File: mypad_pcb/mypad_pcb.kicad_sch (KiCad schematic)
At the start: 25 parts, among them J1 USB_C_Receptacle_USB2.0, SW1 SW_BOOTMODE, SW2 SW_RESET, U1 FT232RL, U2 AMS1117-3.3, U3 STM32F030K6Tx, Y1 16MHz

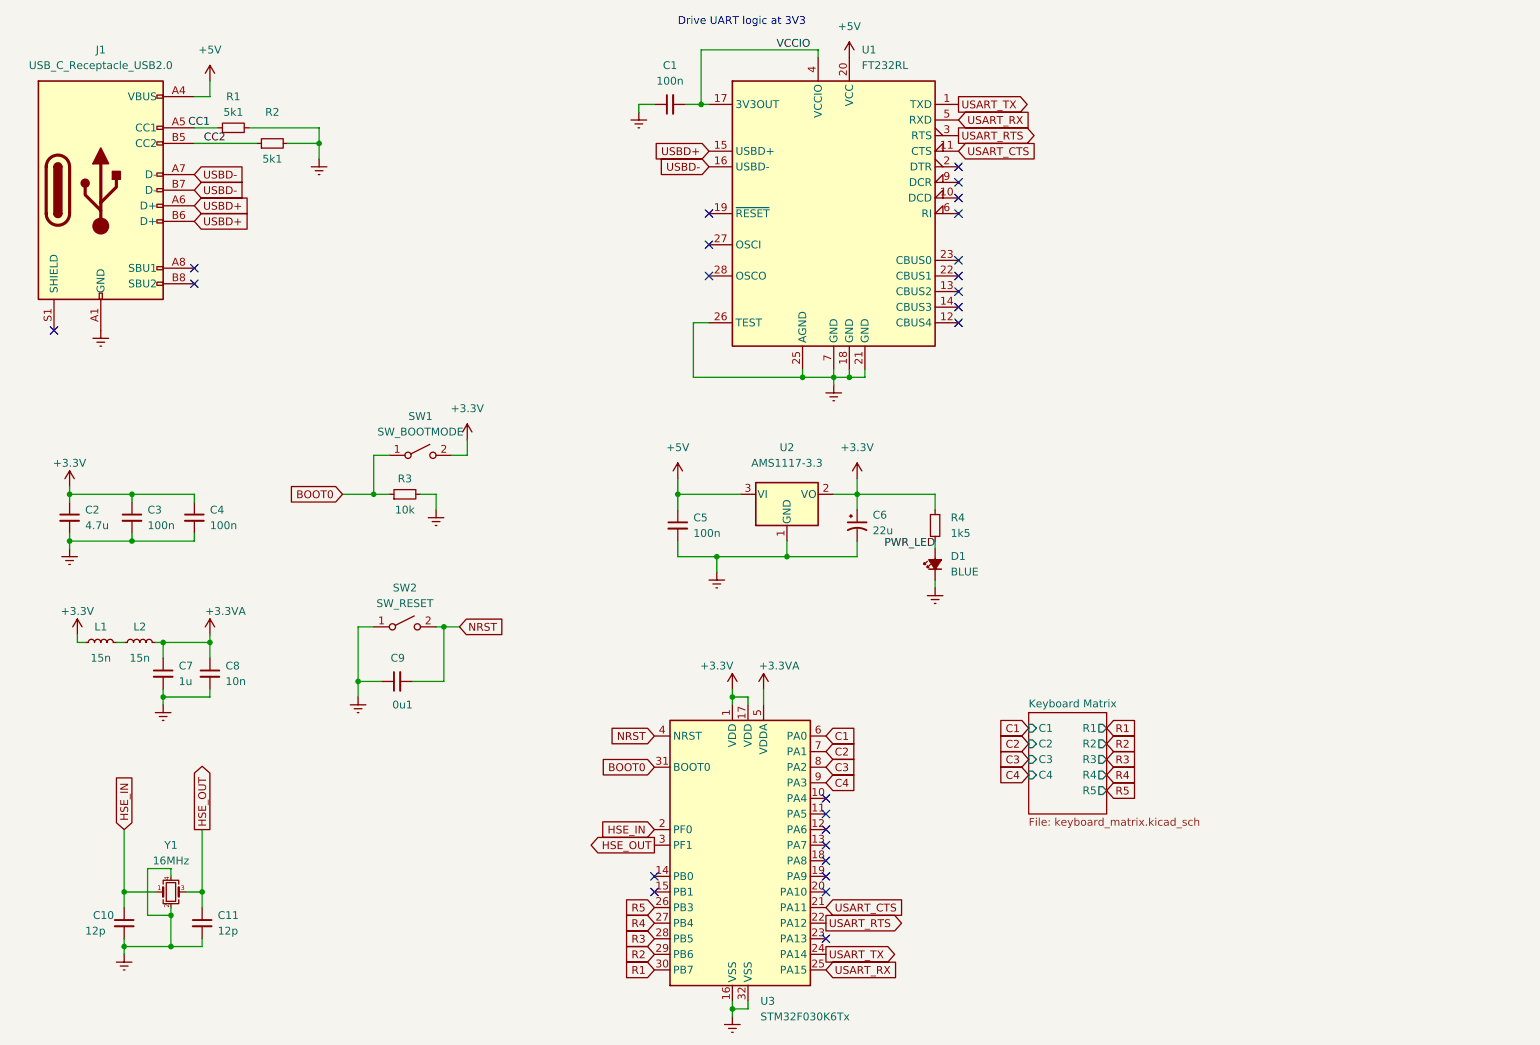
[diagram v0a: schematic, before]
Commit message: Swap components for STM32F042C6 compatible ones
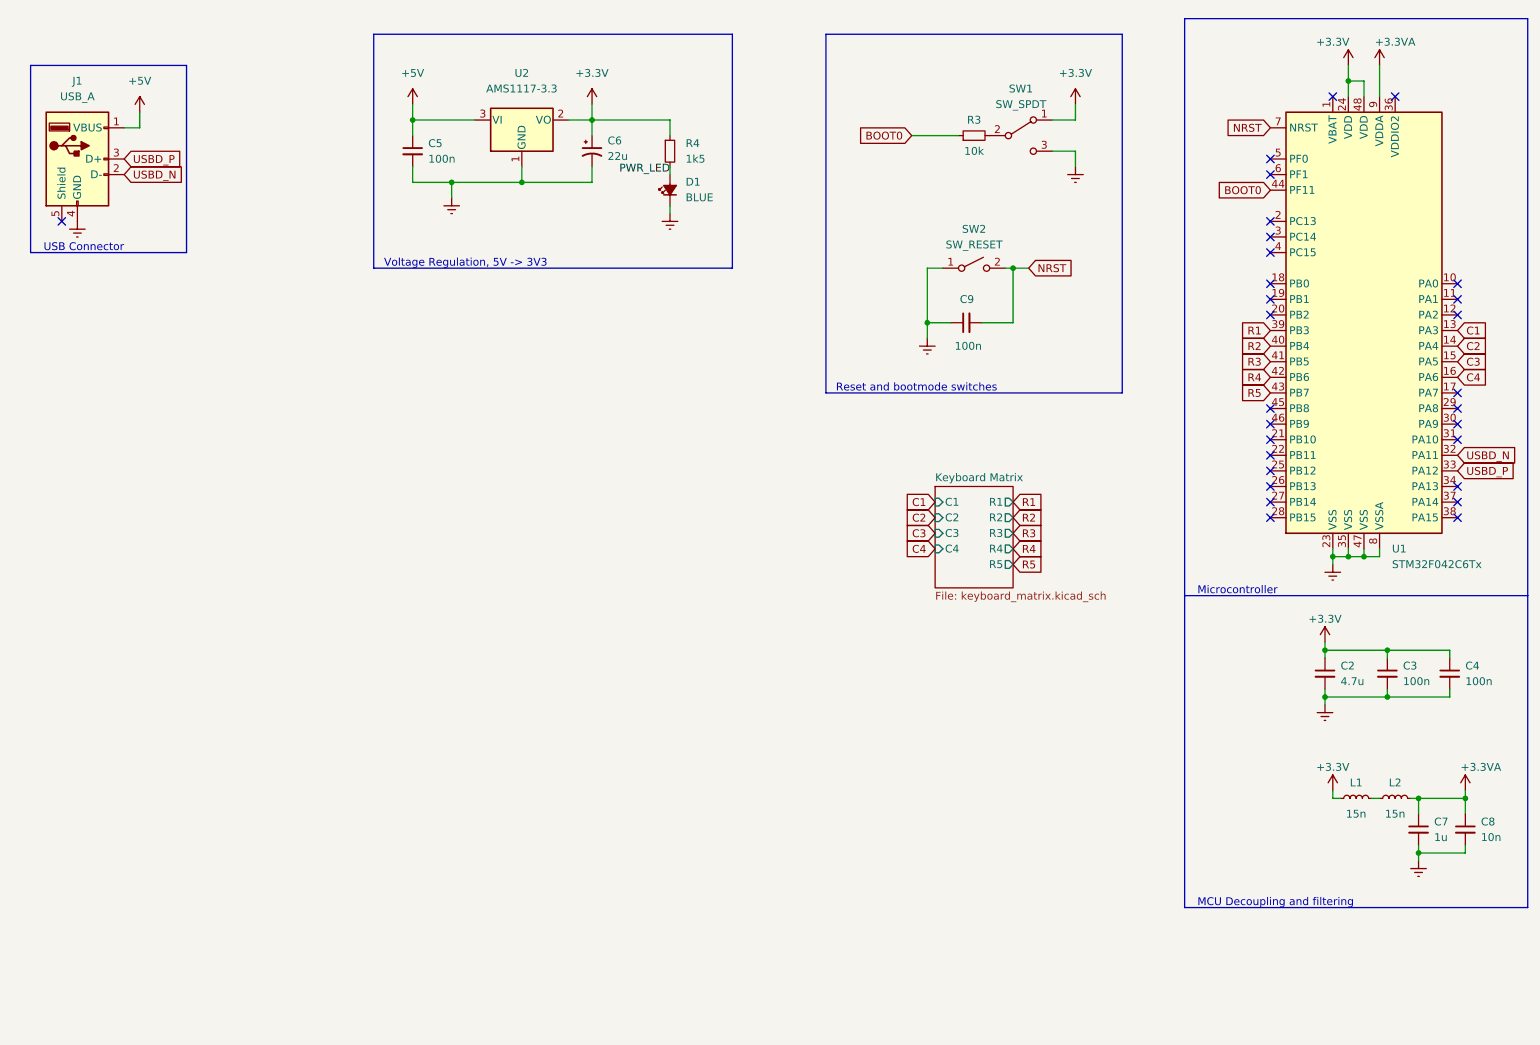
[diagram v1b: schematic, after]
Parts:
- removed C1: 100n, Capacitor_SMD:C_0603_1608Metric, symbol Device:C_Small
- removed C10, C11: 12p, Capacitor_SMD:C_0603_1608Metric, symbol Device:C_Small
- removed J1: USB_C_Receptacle_USB2.0, Connector_USB:USB_C_Receptacle_HRO_TYPE-C-31-M-12, symbol Connector:USB_C_Receptacle_USB2.0
- removed R1, R2: 5k1, Resistor_SMD:R_0603_1608Metric, symbol Device:R_Small
- removed SW1: SW_BOOTMODE, Button_Switch_THT:SW_PUSH_6mm, symbol Switch:SW_SPST
- removed U1: FT232RL, Package_SO:SSOP-28_5.3x10.2mm_P0.65mm, symbol Interface_USB:FT232RL
- removed U3: STM32F030K6Tx, Package_QFP:LQFP-32_7x7mm_P0.8mm, symbol MCU_ST_STM32F0:STM32F030K6Tx
- removed Y1: 16MHz, Crystal:Crystal_SMD_3225-4Pin_3.2x2.5mm, symbol Device:Crystal_GND24_Small
- added J1: USB_A, Connector_USB:USB_A_CONNFLY_DS1095-WNR0, symbol Connector:USB_A
- added SW1: SW_SPDT, Button_Switch_THT:ESP_SPDT_Slide_Switch, symbol Switch:SW_SPDT
- added U1: STM32F042C6Tx, Package_QFP:LQFP-48_7x7mm_P0.5mm, symbol MCU_ST_STM32F0:STM32F042C6Tx
- C9: value 0u1 -> 100n
- SW2: footprint Button_Switch_THT:SW_PUSH_6mm -> Button_Switch_SMD:DTSM31N_SMD_Tact_Switch_4.3mm
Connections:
- net +3.3V: now also SW1.1 (A), U1.24 (VDD), U1.48 (VDD)
- net +3.3VA: now also U1.9 (VDDA)
- net +5V: now also J1.1 (VBUS)
- net BOOT0: now also U1.44 (PF11)
- net C1: now also U1.13 (PA3)
- net C2: now also U1.14 (PA4)
- net C3: now also U1.15 (PA5)
- net C4: now also U1.16 (PA6)
- net Earth: now also J1.4 (GND), SW1.3 (C), U1.23 (VSS), U1.35 (VSS), U1.47 (VSS), U1.8 (VSSA); no longer R3.2
- net NRST: now also U1.7 (NRST)
- net R1: now also U1.39 (PB3)
- net R2: now also U1.40 (PB4)
- net R3: now also U1.41 (PB5)
- net R4: now also U1.42 (PB6)
- net R5: now also U1.43 (PB7)
- new net: R3.2, SW1.2 (B)
- new net USBD_N: J1.2 (D-), U1.32 (PA11)
- new net USBD_P: J1.3 (D+), U1.33 (PA12)
- no-connect marks 25 -> 29
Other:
- note added: "MCU Decoupling and filtering"
- note added: "Microcontroller"
- note added: "Reset and bootmode switches"
- note added: "USB Connector"
- note added: "Voltage Regulation, 5V -> 3V3"
- note removed: "Drive UART logic at 3V3"
- moved on the sheet: C2, C3, C4, C5, C6, C7, C8, C9, D1, L1, L2, R3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
